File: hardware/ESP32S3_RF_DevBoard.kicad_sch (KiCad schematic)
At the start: 4 parts, among them J1 USB4105-GF-A, U1 ESD122DMYR

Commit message: continuing to add major block - 5 to 3.3V regulator next. - need to get symbol, footprints, into library now
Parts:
- added D1: LESD5D5.0CT1G, ESP32S3-RF-DevBoard:TVS_LESD5D5.0CT1G, symbol LESD5D5.0CT1G:LESD5D5.0CT1G
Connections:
- net +5V_USB: now also D1.1
- net GND: now also D1.2

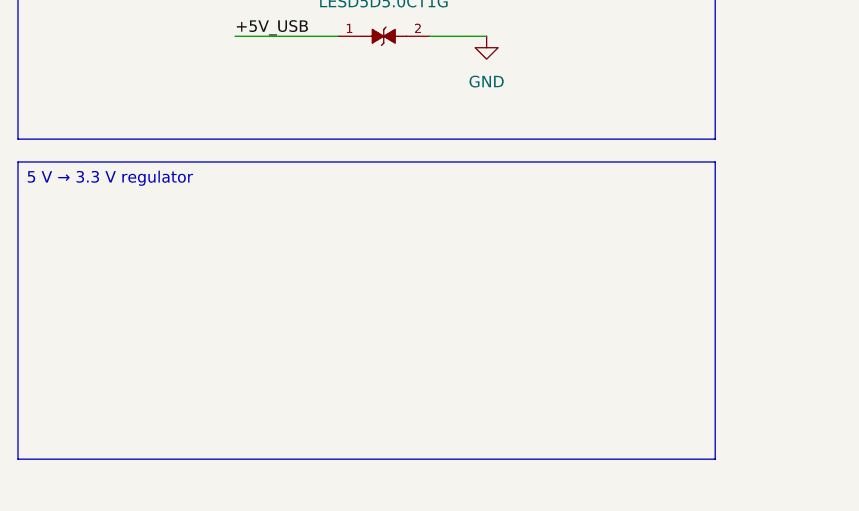
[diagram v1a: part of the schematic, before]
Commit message: working on 5v to 3v3 regulator - reviewing and checking
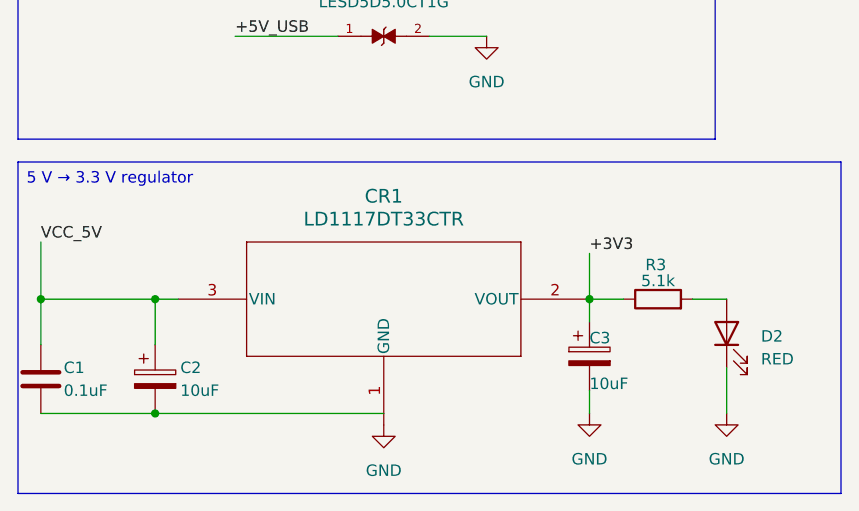
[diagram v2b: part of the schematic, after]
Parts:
- added C1: 0.1uF, Capacitor_SMD:C_0603_1608Metric, symbol Device:C
- added C2, C3: 10uF, Capacitor_Tantalum_SMD:CP_EIA-3528-21_Kemet-B, symbol Device:C_Polarized
- added CR1: LD1117DT33CTR, DPAK_STM, symbol LD1117DT33CTR:LD1117DT33CTR
- added D2: RED, LED_SMD:LED_0603_1608Metric, symbol Device:LED
- added R3: 5.1k, Resistor_SMD:R_0603_1608Metric, symbol Device:R
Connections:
- net GND: now also C3.2, CR1.1 (GND), D2.1 (K)
- new net: C1.2, C2.2
- new net: D2.2 (A), R3.2
- new net +3V3: C3.1, CR1.2 (VOUT), R3.1
- new net VCC_5V: C1.1, C2.1, CR1.3 (VIN)

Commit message: updating
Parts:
- renumbered CR1 to U2
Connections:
- net VCC_5V is gone; now on net +5V_USB: C1.1, C2.1, U2.3 (VIN)
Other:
- note added: "5V input from computer/USB charger"
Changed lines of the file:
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@@
 	(generator_version "10.0")
 	(paper "A4")
+	(text "5V input from computer/USB charger"
+		(exclude_from_sim no)
+		(at 75.438 20.828 0)
+		(effects
+			(font
+				(size 0.762 0.762)
+				(color 255 153 0 1)
+			)
+		)
+	)
 	(text_box "VBUS ESD/TVS protection part\n(ref D8 in devkit)"
 		(exclude_from_sim no)
@@
 		)
 	)
-	(text_box "USB-C Input\n"
+	(text_box "USB-C Input\n(main power source)"
 		(exclude_from_sim no)
 		(at 16.51 15.24 0)
@@
 		)
 	)
-	(label "VCC_5V"
+	(label "+5V_USB"
 		(at 19.05 168.91 0)
 		(effects
@@
 		(dnp no)
 		(fields_autoplaced yes)
-		(property "Reference" "CR1"
+		(property "Reference" "U2"
 			(at 57.15 163.83 0)
 			(show_name no)
@@
 			(project "ESP32S3_RF_DevBoard"
 				(path "/784333dd-3fa1-4922-bbbf-658c1720cebd"
-					(reference "CR1")
+					(reference "U2")
 					(unit 1)
 				)

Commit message: Fixing ERC on the ldo block
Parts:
- U2: footprint DPAK_STM -> ESP32S3-RF-DevBoard:DPAK_STM
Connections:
- net GND: now also C1.2, C2.2
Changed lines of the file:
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@@
-	)
-	(junction
-		(at 31.75 187.96)
-		(diameter 0)
-		(color 0 0 0 0)
 	)
 	(junction
@@
 	)
 	(junction
+		(at 25.4 187.96)
+		(diameter 0)
+		(color 0 0 0 0)
+	)
+	(junction
 		(at 50.8 69.85)
 		(diameter 0)
@@
 	(wire
 		(pts
-			(xy 31.75 187.96) (xy 57.15 187.96)
-		)
-		(stroke
-			(width 0)
-			(type default)
-		)
-	)
-	(wire
-		(pts
 			(xy 73.66 54.61) (xy 74.93 54.61)
 		)
@@
 	(wire
 		(pts
-			(xy 19.05 187.96) (xy 31.75 187.96)
+			(xy 25.4 187.96) (xy 31.75 187.96)
+		)
+		(stroke
+			(width 0)
+			(type default)
+		)
+	)
+	(wire
+		(pts
+			(xy 19.05 187.96) (xy 25.4 187.96)
 		)
 		(stroke
@@
 		(pts
 			(xy 31.75 175.26) (xy 34.29 175.26)
+		)
+		(stroke
+			(width 0)
+			(type default)
+		)
+	)
+	(wire
+		(pts
+			(xy 25.4 187.96) (xy 25.4 189.23)
 		)
 		(stroke
@@
 	)
 	(symbol
+		(lib_id "power:GND")
+		(at 25.4 189.23 0)
+		(unit 1)
+		(body_style 1)
+		(exclude_from_sim no)
+		(in_bom yes)
+		(on_board yes)
+		(in_pos_files yes)
+		(dnp no)
+		(fields_autoplaced yes)
+		(property "Reference" "#PWR010"
+			(at 25.4 195.58 0)
+			(hide yes)
+			(show_name no)
+			(do_not_autoplace no)
+			(effects
+				(font
+					(size 1.27 1.27)
+				)
+			)
+		)
+		(property "Value" "GND"
+			(at 25.4 194.31 0)
+			(show_name no)
+			(do_not_autoplace no)
+			(effects
+				(font
+					(size 1.27 1.27)
+				)
+			)
+		)
+		(property "Footprint" ""
+			(at 25.4 189.23 0)
+			(hide yes)
+			(show_name no)
+			(do_not_autoplace no)
+			(effects
+				(font
+					(size 1.27 1.27)
+				)
+			)
+		)
+		(property "Datasheet" ""
+			(at 25.4 189.23 0)
+			(hide yes)
+			(show_name no)
+			(do_not_autoplace no)
+			(effects
+				(font
+					(size 1.27 1.27)
+				)
+			)
+		)
+		(property "Description" "Power symbol creates a global label with name \"GND\" , ground"
+			(at 25.4 189.23 0)
+			(hide yes)
+			(show_name no)
+			(do_not_autoplace no)
+			(effects
+				(font
+					(size 1.27 1.27)
+				)
+			)
+		)
+		(pin "1"
+		)
+		(instances
+			(project "ESP32S3_RF_DevBoard"
+				(path "/784333dd-3fa1-4922-bbbf-658c1720cebd"
+					(reference "#PWR010")
+					(unit 1)
+				)
+			)
+		)
+	)
+	(symbol
 		(lib_id "Device:R")
 		(at 78.74 54.61 90)
@@
 			)
 		)
-		(property "Footprint" "DPAK_STM"
+		(property "Footprint" "ESP32S3-RF-DevBoard:DPAK_STM"
 			(at 34.29 173.99 0)
 			(hide yes)

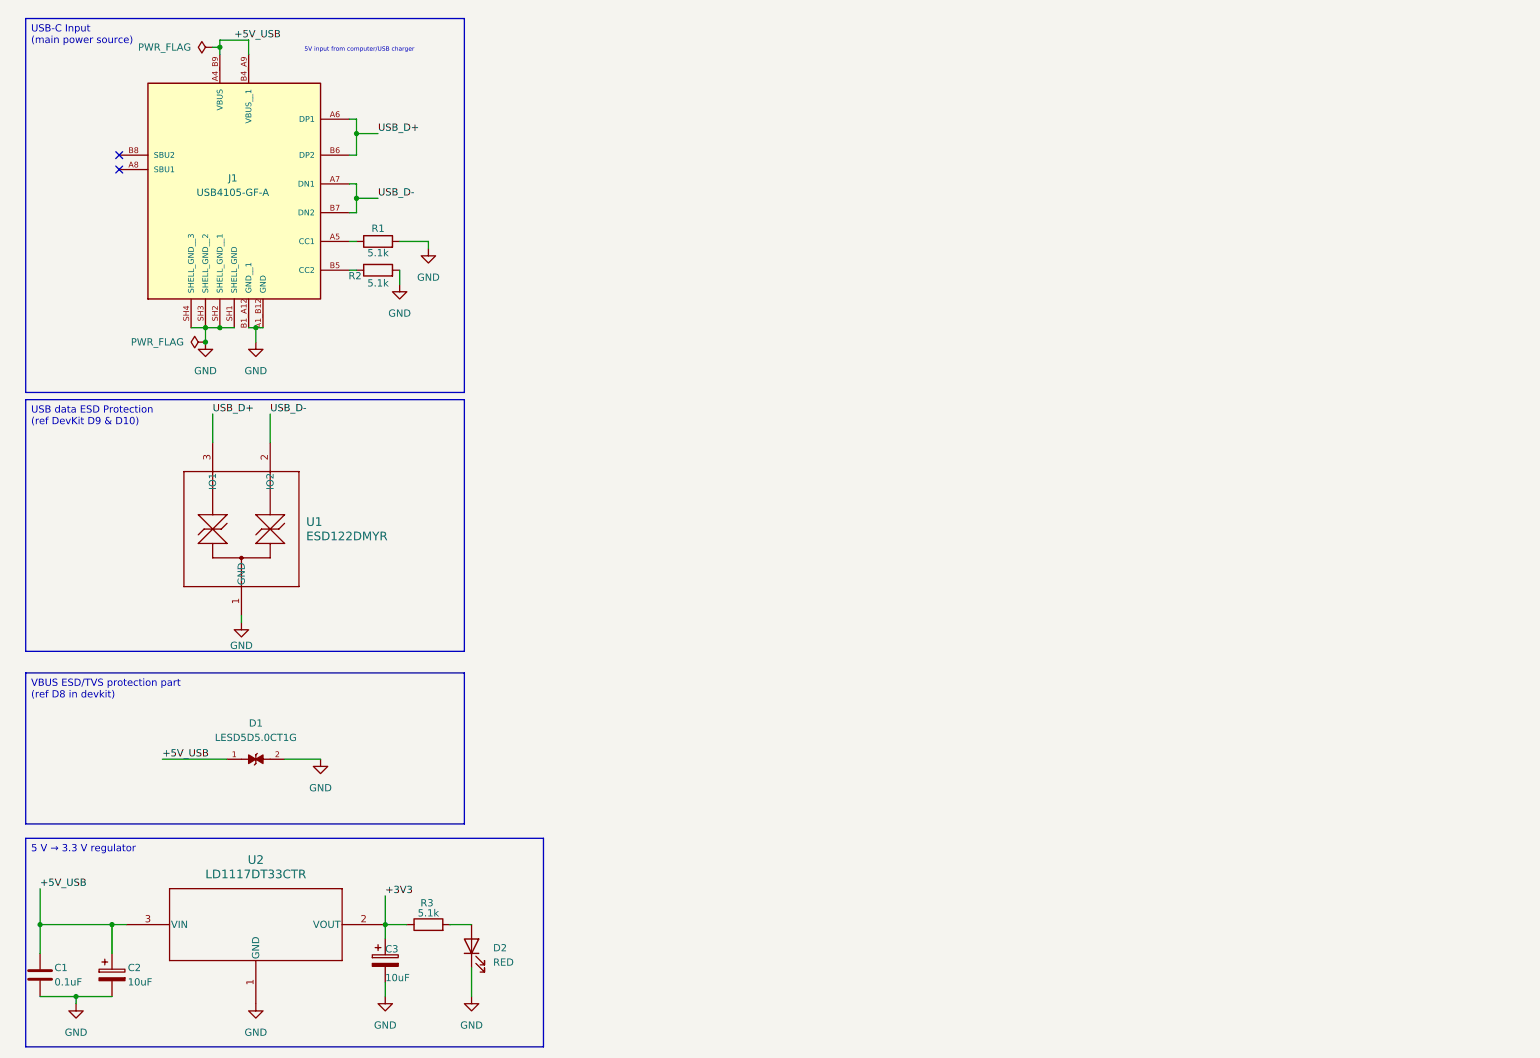
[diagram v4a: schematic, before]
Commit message: adding in the ESP module and switches - need to now go through and add R's on USB traces from the Espresif guide recs
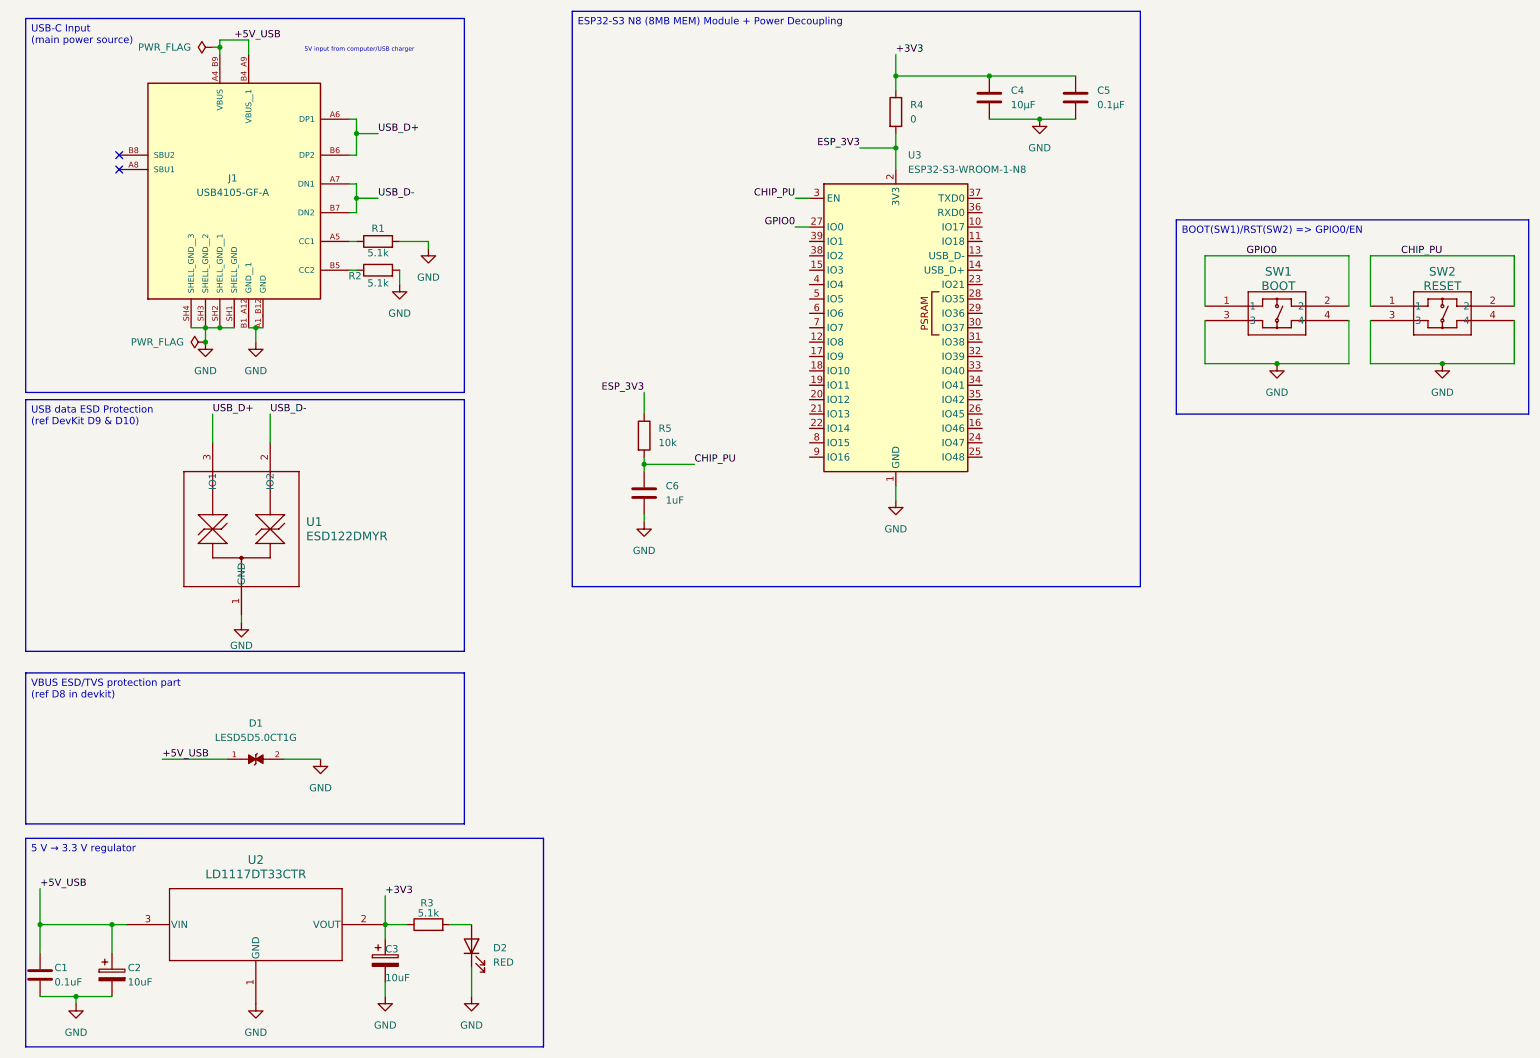
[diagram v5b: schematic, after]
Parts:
- added C4: 10µF, Capacitor_SMD:C_0603_1608Metric, symbol Device:C
- added C5: 0.1µF, Capacitor_SMD:C_0603_1608Metric, symbol Device:C
- added C6: 1uF, Capacitor_SMD:C_0805_2012Metric, symbol Device:C
- added R4: 0, Resistor_SMD:R_0603_1608Metric, symbol Device:R
- added R5: 10k, Resistor_SMD:R_0805_2012Metric, symbol Device:R
- added SW1: BOOT, ESP32S3-RF-DevBoard:SKRPANE010_AAL, symbol SKRPANE010:SKRPANE010
- added SW2: RESET, ESP32S3-RF-DevBoard:SKRPANE010_AAL, symbol SKRPANE010:SKRPANE010
- added U3: ESP32-S3-WROOM-1-N8, RF_Module:ESP32-S3-WROOM-1, symbol RF_Module:ESP32-S3-WROOM-1
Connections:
- net +3V3: now also C4.1, C5.1, R4.1
- net GND: now also C4.2, C5.2, C6.2, SW1.3, SW1.4, SW2.3, SW2.4, U3.1 (GND), U3.40 (GND), U3.41 (GND)
- new net CHIP_PU: C6.1, R5.2, SW2.1, SW2.2, U3.3 (EN)
- new net ESP_3V3: R4.2, R5.1, U3.2 (3V3)
- new net GPIO0: SW1.1, SW1.2, U3.27 (IO0)

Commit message: now working on the 1x22 headers
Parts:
- added J2, J3: Conn_01x22, Connector_PinHeader_2.54mm:PinHeader_1x22_P2.54mm_Vertical, symbol Connector_Generic:Conn_01x22
- added LED1: XL-2121RGBC-WS2812B, easyeda:LED-SMD_4P-L2.1-W2.1-BR_XL-2121RGBC-WS2812B, symbol easyeda:XL-2121RGBC-WS2812B
- added R6, R7: 22R, Resistor_SMD:R_0603_1608Metric, symbol Device:R
- added R8: 0R, Resistor_SMD:R_0603_1608Metric, symbol Device:R
- R4: value 0 -> 0R
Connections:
- net +3V3: now also J2.1 (Pin_1), J2.2 (Pin_2), LED1.2 (VDD)
- net +5V_USB: now also J2.21 (Pin_21)
- net CHIP_PU: now also J2.3 (Pin_3)
- net GND: now also J2.22 (Pin_22), J3.1 (Pin_1), LED1.4 (GND)
- net USB_D+: now also R7.2
- net USB_D-: now also R6.2
- net GPIO17: now reaches U3.10 (IO17)
- net GPIO17: now also J2.10 (Pin_10)
- net GPIO18: now reaches U3.11 (IO18)
- net GPIO18: now also J2.11 (Pin_11)
- net GPIO8: now reaches U3.12 (IO8)
- net GPIO8: now also J2.12 (Pin_12)
- net USB_D-_ESP: now reaches U3.13 (USB_D-)
- net USB_D-_ESP: now also R6.1
- net USB_D+_ESP: now reaches U3.14 (USB_D+)
- net USB_D+_ESP: now also R7.1
- net GPIO3: now reaches U3.15 (IO3)
- net GPIO3: now also J2.13 (Pin_13)
- net GPIO46: now reaches U3.16 (IO46)
- net GPIO46: now also J2.14 (Pin_14)
- net GPIO9: now reaches U3.17 (IO9)
- net GPIO9: now also J2.15 (Pin_15)
- net GPIO10: now reaches U3.18 (IO10)
- net GPIO10: now also J2.16 (Pin_16)
- net GPIO11: now reaches U3.19 (IO11)
- net GPIO11: now also J2.17 (Pin_17)
- net GPIO12: now reaches U3.20 (IO12)
- net GPIO12: now also J2.18 (Pin_18)
- net GPIO13: now reaches U3.21 (IO13)
- net GPIO13: now also J2.19 (Pin_19)
- net GPIO14: now reaches U3.22 (IO14)
- net GPIO14: now also J2.20 (Pin_20)
- net GPIO21: now reaches U3.23 (IO21)
- net GPIO47: now reaches U3.24 (IO47)
- net GPIO48: now reaches U3.25 (IO48)
- net GPIO45: now reaches U3.26 (IO45)
- net GPIO35: now reaches U3.28 (IO35)
- net GPIO36: now reaches U3.29 (IO36)
- net GPIO37: now reaches U3.30 (IO37)
- net GPIO38: now reaches U3.31 (IO38)
- net GPIO38: now also R8.2
- net GPIO39: now reaches U3.32 (IO39)
- net GPIO40: now reaches U3.33 (IO40)
- net GPIO41: now reaches U3.34 (IO41)
- net GPIO42: now reaches U3.35 (IO42)
- net RX: now reaches U3.36 (RXD0)
- net TX: now reaches U3.37 (TXD0)
- net GPIO2: now reaches U3.38 (IO2)
- net GPIO1: now reaches U3.39 (IO1)
- net GPIO4: now reaches U3.4 (IO4)
- net GPIO4: now also J2.4 (Pin_4)
- net GPIO5: now reaches U3.5 (IO5)
- net GPIO5: now also J2.5 (Pin_5)
- net GPIO6: now reaches U3.6 (IO6)
- net GPIO6: now also J2.6 (Pin_6)
- net GPIO7: now reaches U3.7 (IO7)
- net GPIO7: now also J2.7 (Pin_7)
- net GPIO15: now reaches U3.8 (IO15)
- net GPIO15: now also J2.8 (Pin_8)
- net GPIO16: now reaches U3.9 (IO16)
- net GPIO16: now also J2.9 (Pin_9)
- new net: LED1.1 (DIN), R8.1
- no-connect marks 2 -> 3
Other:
- note added: "Can program color/stats using ESP32 GPIO38"
- note added: "N8 version does not use PSRAM GPIO Availiable"
- moved on the sheet: C4, C5, C6, R4, R5, SW1, SW2, U3
